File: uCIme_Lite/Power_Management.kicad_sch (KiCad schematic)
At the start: 22 parts, among them J1 USB_MODE, J10 JACK_MODE, Q1 BSS138, Q2 BUK7M27-80EX, Q3 BUK7M27-80EX, Q4 BSS138, U1 LM74502, U2 LM74502

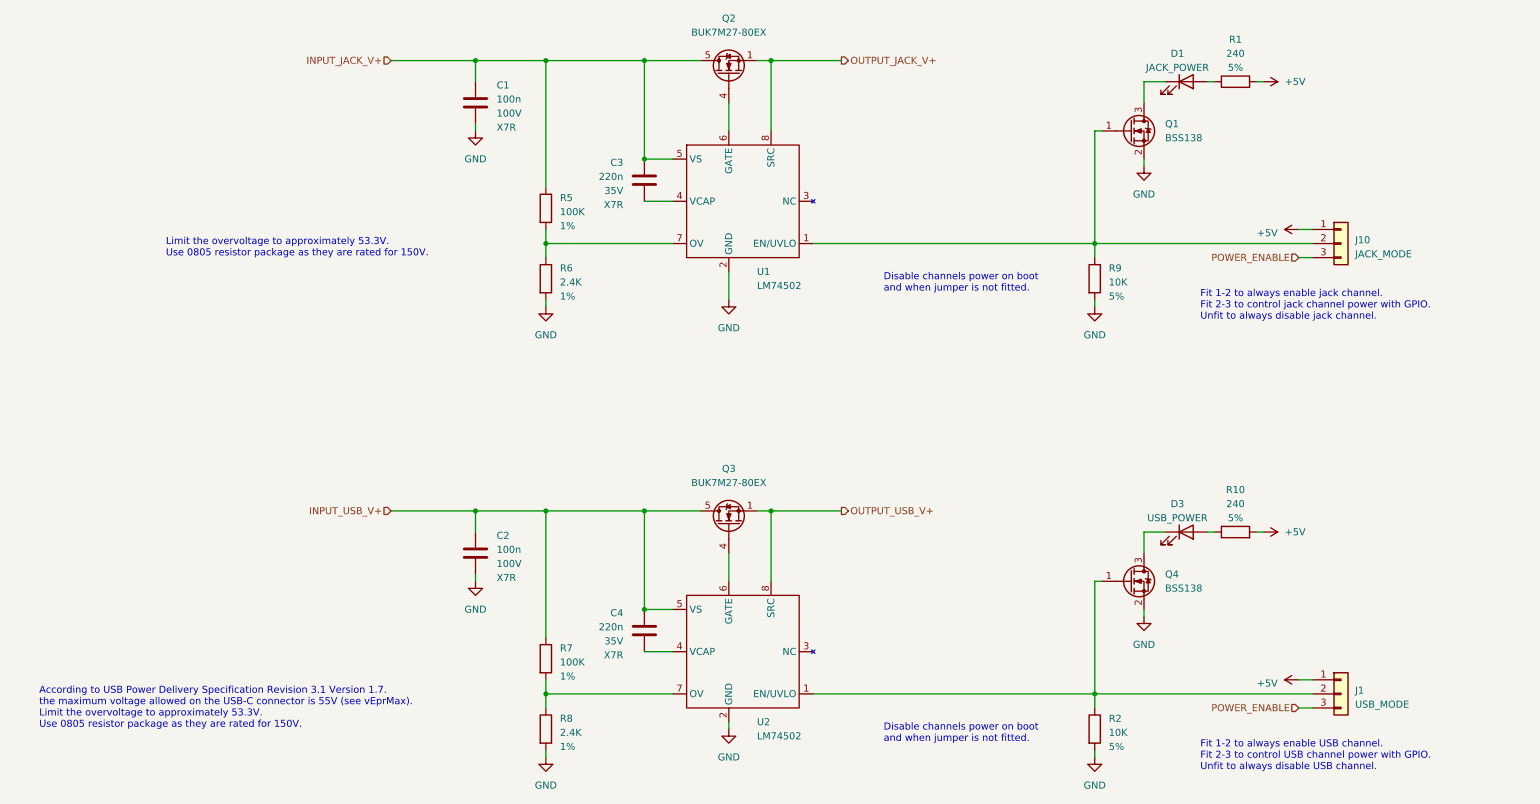
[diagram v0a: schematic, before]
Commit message: lite: Merged jack and USB power modes single-row pin headers into a double-row pin header to save some space on the PCB, currently only the schematic is updated.
Signed-off-by: Adrien Ricciardi <aricciardi@baylibre.com>
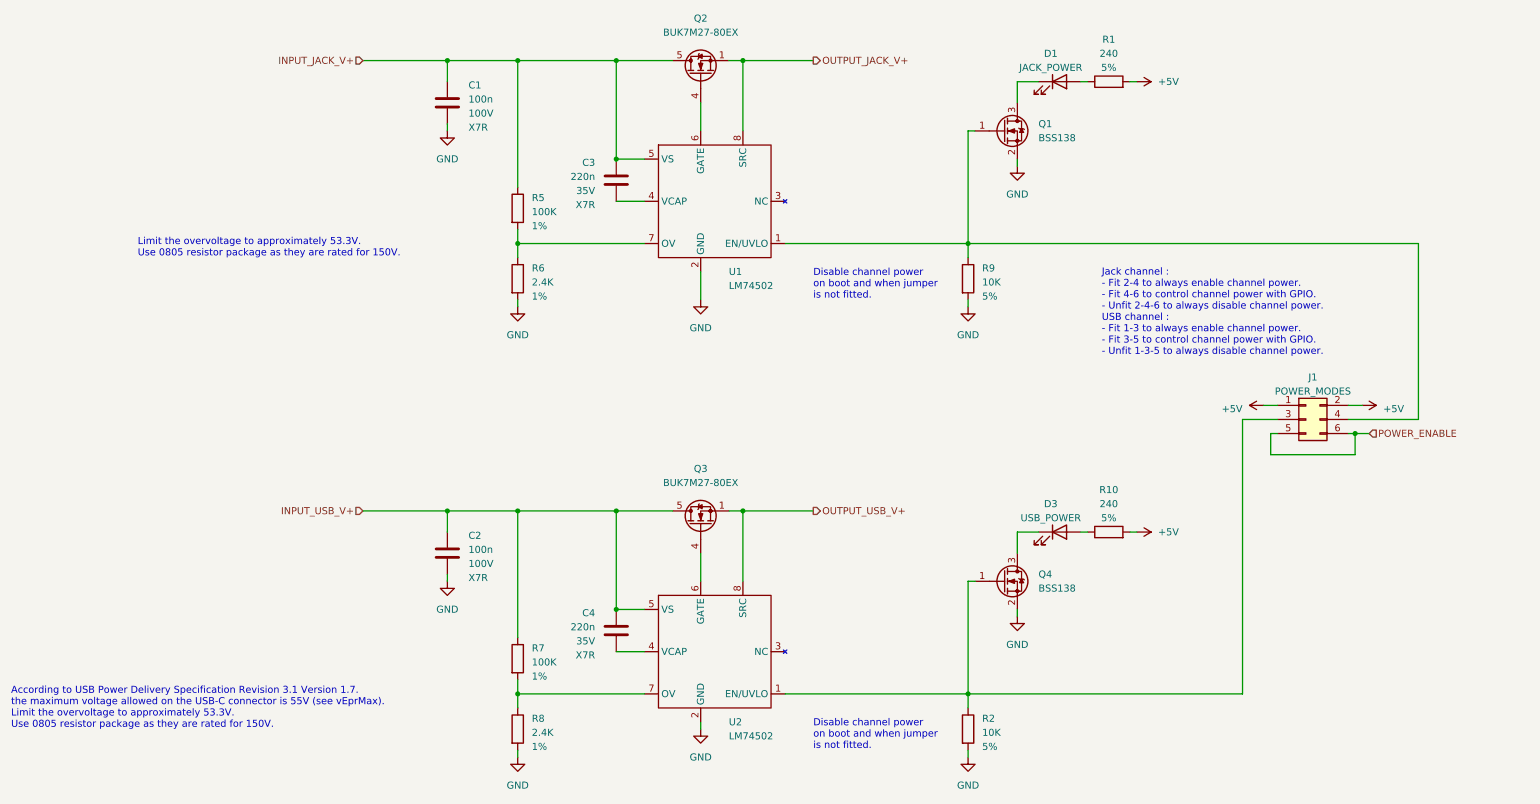
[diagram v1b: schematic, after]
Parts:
- removed J10: JACK_MODE, Connector_PinHeader_2.54mm:PinHeader_1x03_P2.54mm_Horizontal, symbol Connector_Generic:Conn_01x03
- J1: value USB_MODE -> POWER_MODES; footprint Connector_PinHeader_2.54mm:PinHeader_1x03_P2.54mm_Horizontal -> Connector_PinHeader_2.54mm:PinHeader_2x03_P2.54mm_Horizontal; symbol Connector_Generic:Conn_01x03 -> Connector_Generic:Conn_02x03_Odd_Even
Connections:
- net +5V: now also J1.2 (Pin_2)
- net POWER_ENABLE: now also J1.5 (Pin_5), J1.6 (Pin_6); no longer J1.3 (Pin_3)
- net at Q1.1 (G), R9.1, U1.1 (EN/UVLO): now also J1.4 (Pin_4)
- net at Q4.1 (G), R2.1, U2.1 (EN/UVLO): now also J1.3 (Pin_3); no longer J1.2 (Pin_2)
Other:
- note added: "Disable channel power on boot and when jumper is not fitted."
- note added: "Jack channel : - Fit 2-4 to always enable channel power. - Fit 4-6 to control channel power with GPIO. - Unfit 2-4-6 to always disable channel power. USB channel : - Fit 1-3 to always enable channel power. - Fit 3-5 to control channel power with GPIO. - Unfit 1-3-5 to always disable channel power."
- note removed: "Disable channels power on boot and when jumper is not fitted."
- note removed: "Fit 1-2 to always enable USB channel. Fit 2-3 to control USB channel power with GPIO. Unfit to always disable USB channel."
- note removed: "Fit 1-2 to always enable jack channel. Fit 2-3 to control jack channel power with GPIO. Unfit to always disable jack channel."
- moved on the sheet: C1, C2, C3, C4, D1, D3, Q1, Q2, Q3, Q4, R1, R10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

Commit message: lite: Added Aisler part number properties in both schematic and PCB.
Signed-off-by: Adrien Ricciardi <aricciardi@baylibre.com>
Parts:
- C1, C2: AISLER_MPN (none) -> 100n 100V X7R 0805
- C3, C4: AISLER_MPN (none) -> 220n 35V X7R 0805
- D1, D3: AISLER_MPN (none) -> 150080SS75000
- Q1, Q4: AISLER_MPN (none) -> BSS138P,215
- Q2, Q3: AISLER_MPN (none) -> BUK7M27-80EX
- R1, R10: AISLER_MPN (none) -> 240 5% 1206
- R2, R9: AISLER_MPN (none) -> 10K 1% 0603
- R5, R7: AISLER_MPN (none) -> 100K 1% 0805
- R6, R8: AISLER_MPN (none) -> 2.4K 1% 0805
- U1, U2: AISLER_MPN (none) -> LM74502DDFR
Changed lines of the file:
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@@
       (effects (font (size 1.27 1.27)) (justify right))
     )
+    (property "AISLER_MPN" "220n 35V X7R 0805" (at 127 130.81 0)
+      (effects (font (size 1.27 1.27)) hide)
+    )
     (pin "1")
     (pin "2")
@@
     (property "Value2" "1%" (at 111.76 151.765 0)
       (effects (font (size 1.27 1.27)) (justify left))
+    )
+    (property "AISLER_MPN" "2.4K 1% 0805" (at 109.22 148.59 0)
+      (effects (font (size 1.27 1.27)) hide)
     )
     (pin "1")
@@
     )
     (property "PartNumber" "BUK7M27-80EX" (at 142.24 111.76 0)
+      (effects (font (size 1.27 1.27)) hide)
+    )
+    (property "AISLER_MPN" "BUK7M27-80EX" (at 142.24 111.76 0)
       (effects (font (size 1.27 1.27)) hide)
     )
@@
       (effects (font (size 1.27 1.27)) hide)
     )
+    (property "AISLER_MPN" "BSS138P,215" (at 196.85 40.64 0)
+      (effects (font (size 1.27 1.27)) hide)
+    )
     (pin "1")
     (pin "2")
@@
       (effects (font (size 1.27 1.27)) (justify right))
     )
+    (property "AISLER_MPN" "220n 35V X7R 0805" (at 127 49.53 0)
+      (effects (font (size 1.27 1.27)) hide)
+    )
     (pin "1")
     (pin "2")
@@
       (effects (font (size 1.27 1.27)))
     )
+    (property "AISLER_MPN" "240 5% 1206" (at 215.9 31.75 0)
+      (effects (font (size 1.27 1.27)) hide)
+    )
     (pin "1")
     (pin "2")
@@
     (property "Value3" "X7R" (at 100.33 40.005 0)
       (effects (font (size 1.27 1.27)) (justify left))
+    )
+    (property "AISLER_MPN" "100n 100V X7R 0805" (at 96.52 35.56 0)
+      (effects (font (size 1.27 1.27)) hide)
     )
     (pin "1")
@@
     )
     (property "PartNumber" "LM74502DDFR" (at 144.78 134.62 0)
+      (effects (font (size 1.27 1.27)) hide)
+    )
+    (property "AISLER_MPN" "LM74502DDFR" (at 144.78 134.62 0)
       (effects (font (size 1.27 1.27)) hide)
     )
@@
       (effects (font (size 1.27 1.27)) hide)
     )
+    (property "AISLER_MPN" "150080SS75000" (at 207.01 31.75 0)
+      (effects (font (size 1.27 1.27)) hide)
+    )
     (pin "1")
     (pin "2")
@@
       (effects (font (size 1.27 1.27)) hide)
     )
+    (property "AISLER_MPN" "150080SS75000" (at 207.01 113.03 0)
+      (effects (font (size 1.27 1.27)) hide)
+    )
     (pin "1")
     (pin "2")
@@
     (property "Value2" "5%" (at 193.04 151.765 0)
       (effects (font (size 1.27 1.27)) (justify left))
+    )
+    (property "AISLER_MPN" "10K 1% 0603" (at 190.5 148.59 0)
+      (effects (font (size 1.27 1.27)) hide)
     )
     (pin "1")
@@
     )
     (property "PartNumber" "LM74502DDFR" (at 144.78 53.34 0)
+      (effects (font (size 1.27 1.27)) hide)
+    )
+    (property "AISLER_MPN" "LM74502DDFR" (at 144.78 53.34 0)
       (effects (font (size 1.27 1.27)) hide)
     )
@@
       (effects (font (size 1.27 1.27)) (justify left))
     )
+    (property "AISLER_MPN" "100n 100V X7R 0805" (at 96.52 116.84 0)
+      (effects (font (size 1.27 1.27)) hide)
+    )
     (pin "1")
     (pin "2")
@@
       (effects (font (size 1.27 1.27)) (justify left))
     )
+    (property "AISLER_MPN" "2.4K 1% 0805" (at 109.22 67.31 0)
+      (effects (font (size 1.27 1.27)) hide)
+    )
     (pin "1")
     (pin "2")
@@
       (effects (font (size 1.27 1.27)) (justify left))
     )
+    (property "AISLER_MPN" "100K 1% 0805" (at 109.22 135.89 0)
+      (effects (font (size 1.27 1.27)) hide)
+    )
     (pin "1")
     (pin "2")
@@
     (property "Value2" "1%" (at 111.76 57.785 0)
       (effects (font (size 1.27 1.27)) (justify left))
+    )
+    (property "AISLER_MPN" "100K 1% 0805" (at 109.22 54.61 0)
+      (effects (font (size 1.27 1.27)) hide)
     )
     (pin "1")
@@
     )
     (property "PartNumber" "BUK7M27-80EX" (at 142.24 30.48 0)
+      (effects (font (size 1.27 1.27)) hide)
+    )
+    (property "AISLER_MPN" "BUK7M27-80EX" (at 142.24 30.48 0)
       (effects (font (size 1.27 1.27)) hide)
     )
@@
       (effects (font (size 1.27 1.27)) hide)
     )
+    (property "AISLER_MPN" "BSS138P,215" (at 196.85 121.92 0)
+      (effects (font (size 1.27 1.27)) hide)
+    )
     (pin "1")
     (pin "2")
@@
       (effects (font (size 1.27 1.27)))
     )
+    (property "AISLER_MPN" "240 5% 1206" (at 215.9 113.03 0)
+      (effects (font (size 1.27 1.27)) hide)
+    )
     (pin "1")
     (pin "2")
@@
       (effects (font (size 1.27 1.27)) (justify left))
     )
-    (pin "1")
+    (property "AISLER_MPN" "10K 1% 0603" (at 190.5 67.31 0)
+      (effects (font (size 1.27 1.27)) hide)
+    )
+    (pin "1")
